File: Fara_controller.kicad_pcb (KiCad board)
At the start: 2 copper layers, 64.5 x 82.7 mm, 93 parts, among them U1 XL1509-12, U2 XL1509-05, U3 TPS61165DBV, U4 TPS61165DBV, U6 TPS61165DBV, U7 TPS61165DBV, X1 Conn_01x02, X10 Conn_01x02, X11 Conn_01x02, X12 Conn_01x02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

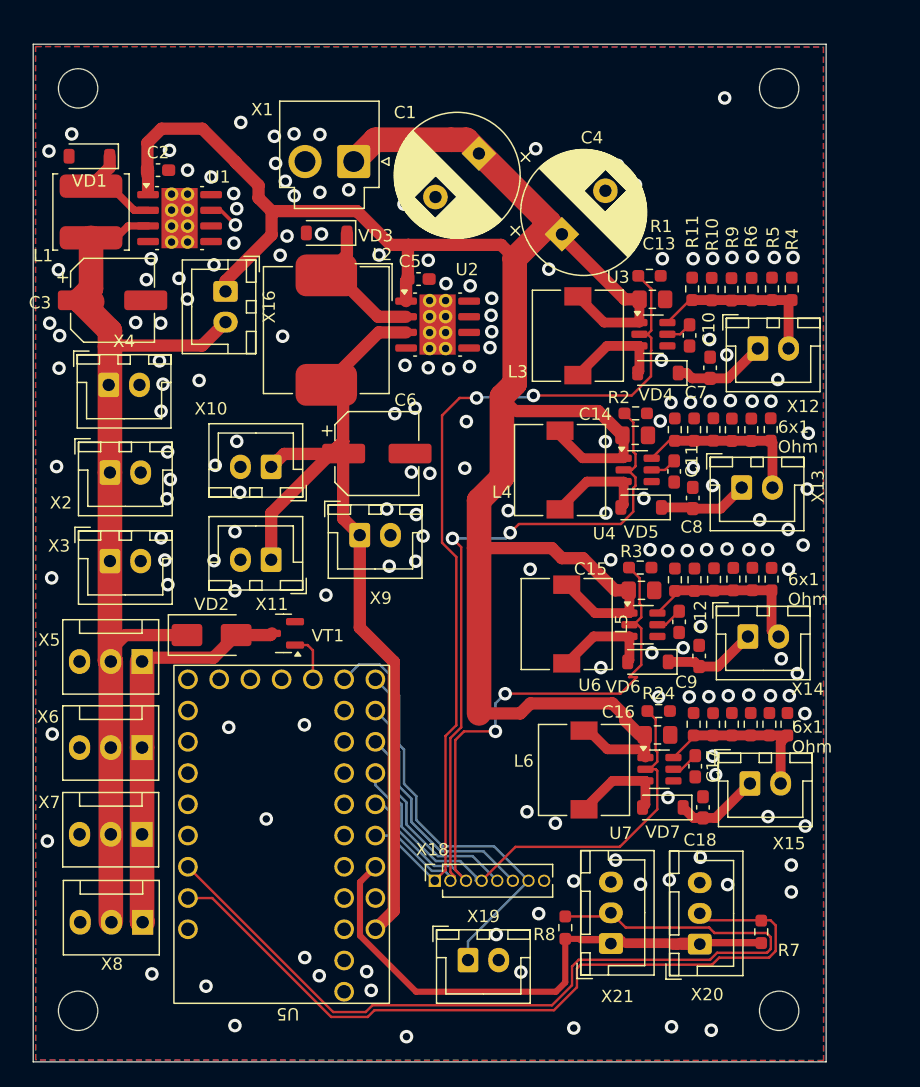
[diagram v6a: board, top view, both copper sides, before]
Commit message: v0.8 compact buck converters were added
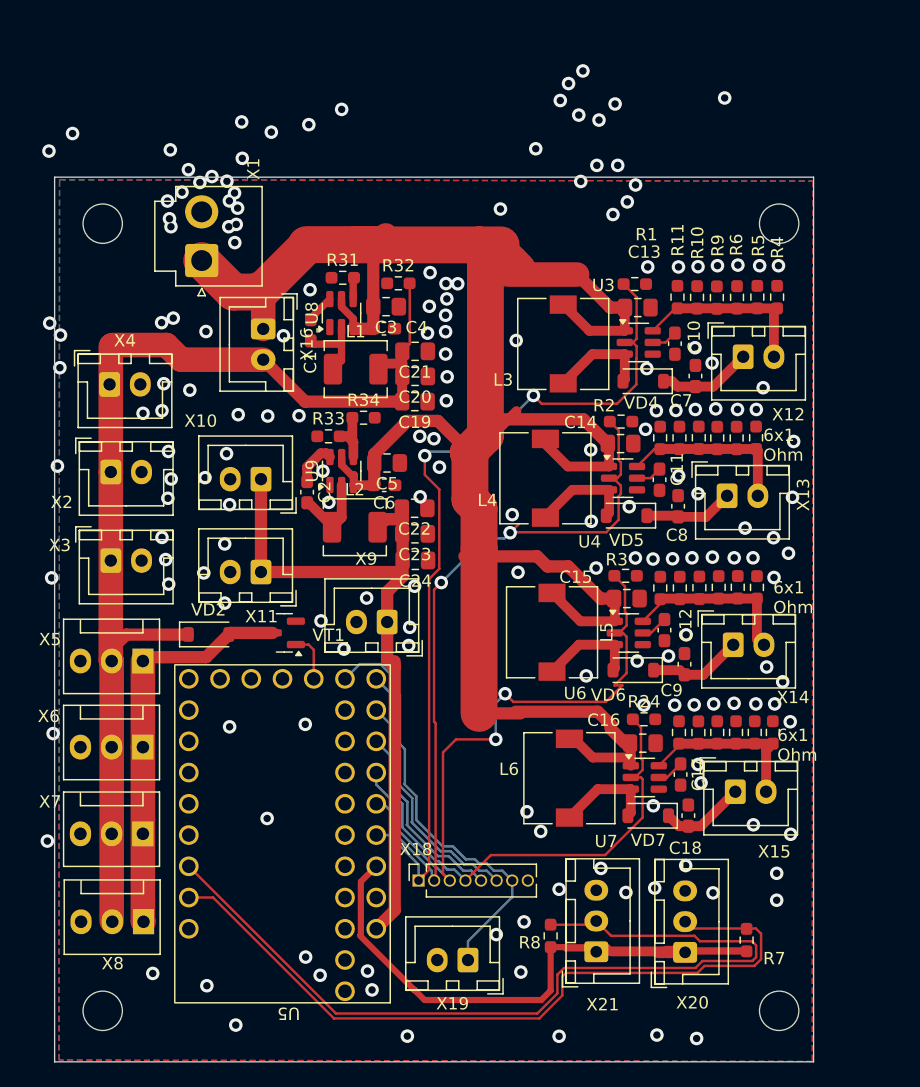
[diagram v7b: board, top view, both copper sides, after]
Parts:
- removed U1: XL1509-12, Package_SO:SOIC-8-1EP_3.9x4.9mm_P1.27mm_EP2.95x4.9mm_Mask2.71x3.4mm_ThermalVias
- removed U2: XL1509-05, Package_SO:SOIC-8-1EP_3.9x4.9mm_P1.27mm_EP2.95x4.9mm_Mask2.71x3.4mm_ThermalVias
- removed VD1, VD3: CDBA3100-HF, Diode_SMD:D_SOD-123
- added C19: 22uF, Capacitor_SMD:C_0805_2012Metric_Pad1.18x1.45mm_HandSolder, F.Cu at (59.4, 51.5)
- added C20: 22uF, Capacitor_SMD:C_0805_2012Metric_Pad1.18x1.45mm_HandSolder, F.Cu at (59.4, 49.4)
- added C21: 22uF, Capacitor_SMD:C_0805_2012Metric_Pad1.18x1.45mm_HandSolder, F.Cu at (59.4, 47.4)
- added C22: 22uF, Capacitor_SMD:C_0805_2012Metric_Pad1.18x1.45mm_HandSolder, F.Cu at (59.4, 60.1)
- added C23: 22uF, Capacitor_SMD:C_0805_2012Metric_Pad1.18x1.45mm_HandSolder, F.Cu at (59.4, 62.2)
- added C24: 22uF, Capacitor_SMD:C_0805_2012Metric_Pad1.18x1.45mm_HandSolder, F.Cu at (59.4, 64.4)
- added R31: 10k, Resistor_SMD:R_0603_1608Metric_Pad0.98x0.95mm_HandSolder, F.Cu at (53.5, 41.4)
- added R32: 54.9k, Resistor_SMD:R_0603_1608Metric_Pad0.98x0.95mm_HandSolder, F.Cu at (58.0, 41.9)
- added R33: 10k, Resistor_SMD:R_0603_1608Metric_Pad0.98x0.95mm_HandSolder, F.Cu at (52.4, 54.3)
- added R34: 54.9k, Resistor_SMD:R_0603_1608Metric_Pad0.98x0.95mm_HandSolder, F.Cu at (55.2, 52.8)
- added U8: TPS563200, Package_TO_SOT_SMD:SOT-23-6, F.Cu at (53.4, 44.3)
- added U9: TPS563200, Package_TO_SOT_SMD:SOT-23-6, F.Cu at (53.4, 57.1)
- C1, C4: value 470uF -> 0.1uF; footprint Capacitor_THT:CP_Radial_D10.0mm_P5.00mm -> Capacitor_SMD:C_0603_1608Metric_Pad1.08x0.95mm_HandSolder
- C2: value 1u -> 0.1uF
- C3: value 180uF -> 22uF; footprint Capacitor_SMD:CP_Elec_6.3x7.7 -> Capacitor_SMD:C_0805_2012Metric_Pad1.18x1.45mm_HandSolder
- C5: value 1u -> 22uF; footprint Capacitor_SMD:C_0603_1608Metric_Pad1.08x0.95mm_HandSolder -> Capacitor_SMD:C_0805_2012Metric_Pad1.18x1.45mm_HandSolder
- C6: value 180uF -> 0.1uF; footprint Capacitor_SMD:CP_Elec_6.3x7.7 -> Capacitor_SMD:C_0603_1608Metric_Pad1.08x0.95mm_HandSolder
- L1: value 150uH -> 4u7; footprint Inductor_SMD:L_TDK_VLS6045EX_VLS6045AF -> Inductor_SMD:L_Chilisin_BMRx00040412
- L2: value 68uH -> 4u7; footprint Inductor_SMD:L_Bourns_SRP1050WA -> Inductor_SMD:L_Chilisin_BMRx00040412
- VD2: footprint Diode_SMD:D_SMA -> Diode_SMD:D_SOD-123
- moved C2 28.8 mm to (50.6, 58.8), turned to -90 degrees
- moved L1 25.0 mm to (54.6, 48.8), turned to 0 degrees
- moved C3 22.2 mm to (57.0, 43.8), turned to 180 degrees
- moved C1 19.8 mm to (50.9, 45.7), turned to -90 degrees
- moved C4 16.4 mm to (56.9, 45.5), turned to 180 degrees
- moved L2 16.2 mm to (54.5, 61.7), turned to 0 degrees
- moved C5 15.2 mm to (57.1, 56.5), turned to 180 degrees
- moved X1 14.8 mm to (42.0, 40.0), turned to 90 degrees
- moved REF** 11.2 mm to (34.0, 37.0)
- moved REF** 11.0 mm to (89.0, 37.0)
- moved X9 7.41 mm to (57.1, 69.4), turned to 180 degrees
- moved X16 4.32 mm to (47.0, 45.6)
- moved C6 2.65 mm to (56.9, 58.3), turned to 180 degrees
- moved REF** 2.00 mm to (34.0, 101.0)
- moved C15 1.37 mm to (76.6, 67.5)
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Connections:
- C1 pad 1: VPP -> Net-(U8-VBST)
- C1 pad 2: GND -> Net-(U8-SW)
- C2 pad 1: VPP -> Net-(U9-VBST)
- C2 pad 2: GND -> Net-(U9-SW)
- C3 pad 1: +12V -> GND
- C3 pad 2: GND -> VPP
- C4 pad 1: VPP -> GND
- C4 pad 2: GND -> VPP
- C5 pad 1: VPP -> GND
- C5 pad 2: GND -> VPP
- C6 pad 1: +5V -> GND
- C6 pad 2: GND -> VPP
- L1 pad 1: Net-(U1-OUT) -> Net-(U8-SW)
- L2 pad 1: Net-(U2-OUT) -> Net-(U9-SW)
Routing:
- net +5V: track 76.4 -> 57.6 mm
- net Net-(U2-OUT): track 12.0 -> 0.00 mm
- net +12V: track 81.1 -> 92.1 mm
- net Net-(U1-OUT): track 8.51 -> 0.00 mm
- net Net-(U9-SW): track 0.00 -> 6.48 mm
- net Net-(U8-SW): track 0.00 -> 6.32 mm
- net Net-(U9-VFB): track 0.00 -> 4.52 mm
- net VPP: track 194.3 -> 189.9 mm
- net Net-(U9-VBST): track 0.00 -> 3.63 mm
- net LEDS2: track 64.0 -> 61.0 mm
- net Net-(U8-VBST): track 0.00 -> 2.32 mm
- net LEDS1: track 73.3 -> 71.2 mm
- net STROBE_INPUT: track 36.9 -> 35.1 mm
- net GND: track 1.86 -> 0.00 mm
- net Net-(U8-VFB): track 0.00 -> 1.76 mm
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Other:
- board size 64.5 x 82.7 mm -> 61.7 x 71.9 mm

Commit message: v0.9 small changes
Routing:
- net +5V: track 57.6 -> 69.0 mm, vias 0 -> 2
- net LEDS1: track 71.2 -> 69.9 mm
